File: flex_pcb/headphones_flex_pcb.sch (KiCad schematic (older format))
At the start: 14 parts, among them J1 LIGHTING_JACK, J3 BOTTOM_FLEX_LIGHTNING, J5 LIGHTNING_HEADPHONE_ADAPTER, J7 IPHONE_HEADPHONE_JACK, J8 CONN_01X02, U1 SN74LVC1G123, U2 ADG774A-LFCSP, U3 SN74LVC1G123, U4 NC7S32-micropak6

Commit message: About to try front fold
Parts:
- removed J8: CONN_01X02, Pin_Headers:Pin_Header_Straight_1x02_Pitch2.54mm, symbol CONN_01X02
- added J?: TEST_1P, symbol TEST_1P
- J3: footprint lightning_flex_pads:LIGHTNING_FLEX_PADS -> lightning_flex_pads:LIGHTNING_FLEX_PADS_NO_CRTYD
- renumbered R3 to R2, R2 to R3
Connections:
- net VCC: now also J?.1
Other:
- note removed: "TODO\nFigure out how to attach power"
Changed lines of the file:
@@
 F 0 "J3" H 9000 2850 60  0000 C CNN
 F 1 "BOTTOM_FLEX_LIGHTNING" H 9050 4050 60  0000 C CNN
-F 2 "lightning_flex_pads:LIGHTNING_FLEX_PADS" H 9000 3650 60  0001 C CNN
+F 2 "lightning_flex_pads:LIGHTNING_FLEX_PADS_NO_CRTYD" H 9000 3650 60  0001 C CNN
 F 3 "" H 9000 3650 60  0001 C CNN
 	1    9000 3650
@@
 $EndComp
 $Comp
-L R R2
+L R R3
 U 1 1 5925BA4D
 P 5250 3100
-F 0 "R2" V 5330 3100 50  0000 C CNN
+F 0 "R3" V 5330 3100 50  0000 C CNN
 F 1 "1M" V 5250 3100 50  0000 C CNN
 F 2 "Resistors_SMD:R_0201_NoSilk" V 5180 3100 50  0001 C CNN
@@
 $EndComp
 $Comp
-L R R3
+L R R2
 U 1 1 59264843
 P 5100 1250
-F 0 "R3" V 5180 1250 50  0000 C CNN
+F 0 "R2" V 5180 1250 50  0000 C CNN
 F 1 "100K" V 5100 1250 50  0000 C CNN
 F 2 "Resistors_SMD:R_0201_NoSilk" V 5030 1250 50  0001 C CNN
@@
 $EndComp
 $Comp
-L CONN_01X02 J8
-U 1 1 5926AC50
-P 9200 1700
-F 0 "J8" H 9200 1850 50  0000 C CNN
-F 1 "CONN_01X02" V 9300 1700 50  0000 C CNN
-F 2 "Pin_Headers:Pin_Header_Straight_1x02_Pitch2.54mm" H 9200 1700 50  0001 C CNN
-F 3 "" H 9200 1700 50  0001 C CNN
-	1    9200 1700
-	1    0    0    -1
-$EndComp
-$Comp
 L VCC #PWR013
 U 1 1 5926ACC1
-P 8900 1550
-F 0 "#PWR013" H 8900 1400 50  0001 C CNN
-F 1 "VCC" H 8900 1700 50  0000 C CNN
-F 2 "" H 8900 1550 50  0001 C CNN
-F 3 "" H 8900 1550 50  0001 C CNN
-	1    8900 1550
-	1    0    0    -1
-$EndComp
-$Comp
-L GNDREF #PWR014
-U 1 1 5926AD08
-P 8900 1850
-F 0 "#PWR014" H 8900 1600 50  0001 C CNN
-F 1 "GNDREF" H 8900 1700 50  0000 C CNN
-F 2 "" H 8900 1850 50  0001 C CNN
-F 3 "" H 8900 1850 50  0001 C CNN
-	1    8900 1850
+P 9800 1550
+F 0 "#PWR013" H 9800 1400 50  0001 C CNN
+F 1 "VCC" H 9800 1700 50  0000 C CNN
+F 2 "" H 9800 1550 50  0001 C CNN
+F 3 "" H 9800 1550 50  0001 C CNN
+	1    9800 1550
 	1    0    0    -1
 $EndComp
@@
 Wire Wire Line
 	2500 2000 3400 2000
-Wire Wire Line
-	8900 1650 8900 1550
-Wire Wire Line
-	9000 1650 8900 1650
-Wire Wire Line
-	8900 1750 8900 1850
-Wire Wire Line
-	9000 1750 8900 1750
 Connection ~ 2050 5850
 Wire Wire Line
@@
 Wire Wire Line
 	8550 3500 8650 3500
-Text Notes 8550 2400 0    89   ~ 0
-TODO\nFigure out how to attach power
 $Comp
 L ADG774A-LFCSP U2
@@
 	-1   0    0    -1
 $EndComp
+$Comp
+L TEST_1P J?
+U 1 1 593E2785
+P 9900 1650
+F 0 "J?" H 9900 1920 50  0000 C CNN
+F 1 "TEST_1P" H 9900 1850 50  0000 C CNN
+F 2 "" H 10100 1650 50  0001 C CNN
+F 3 "" H 10100 1650 50  0001 C CNN
+	1    9900 1650
+	0    1    1    0
+$EndComp
+Wire Wire Line
+	9900 1650 9800 1650
+Wire Wire Line
+	9800 1650 9800 1550
 $EndSCHEMATC

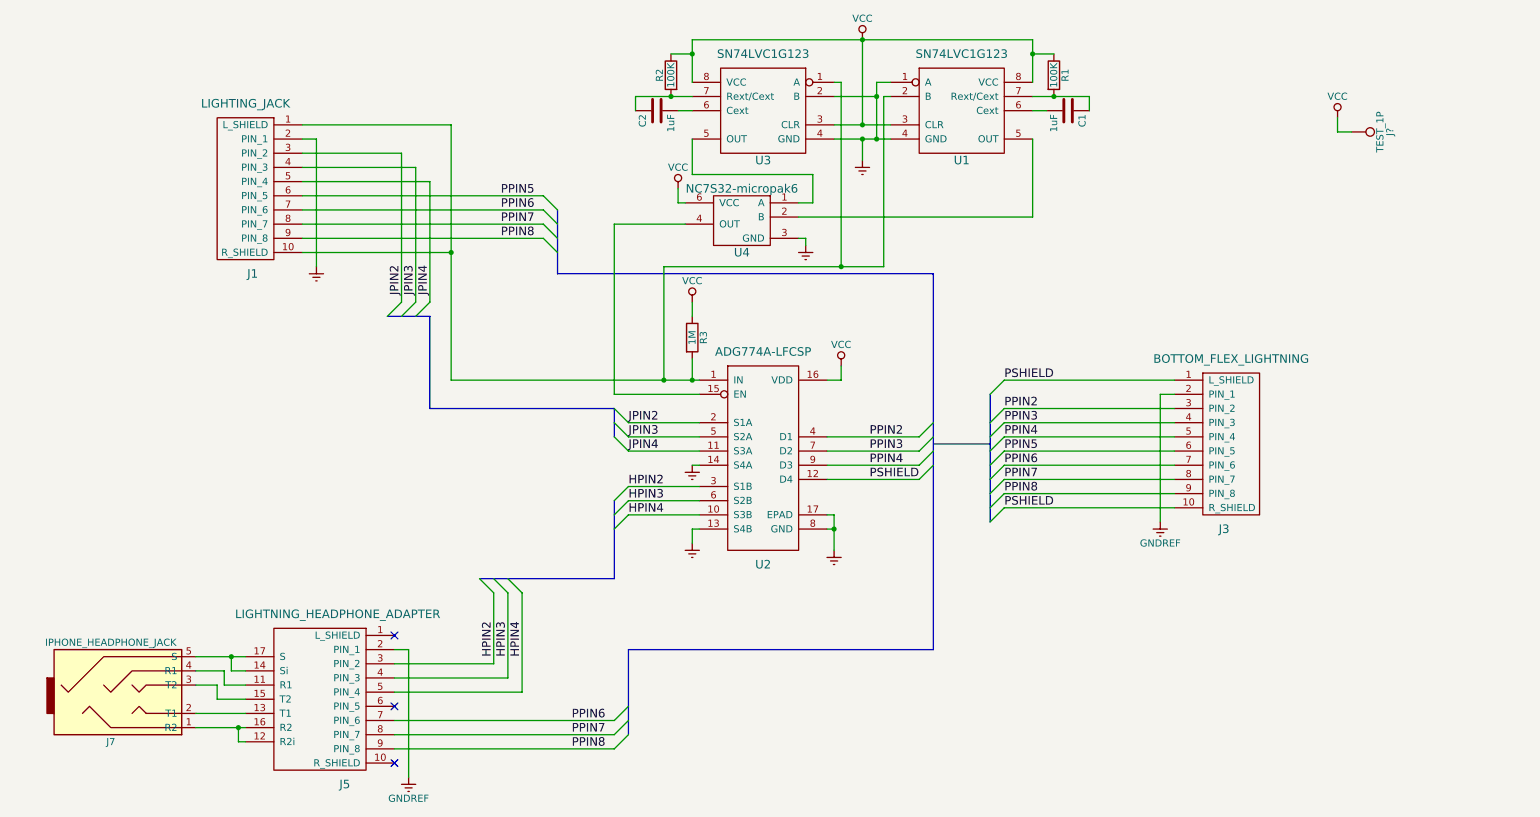
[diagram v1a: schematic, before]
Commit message: WIP: just before switching from 0201 -> 0402
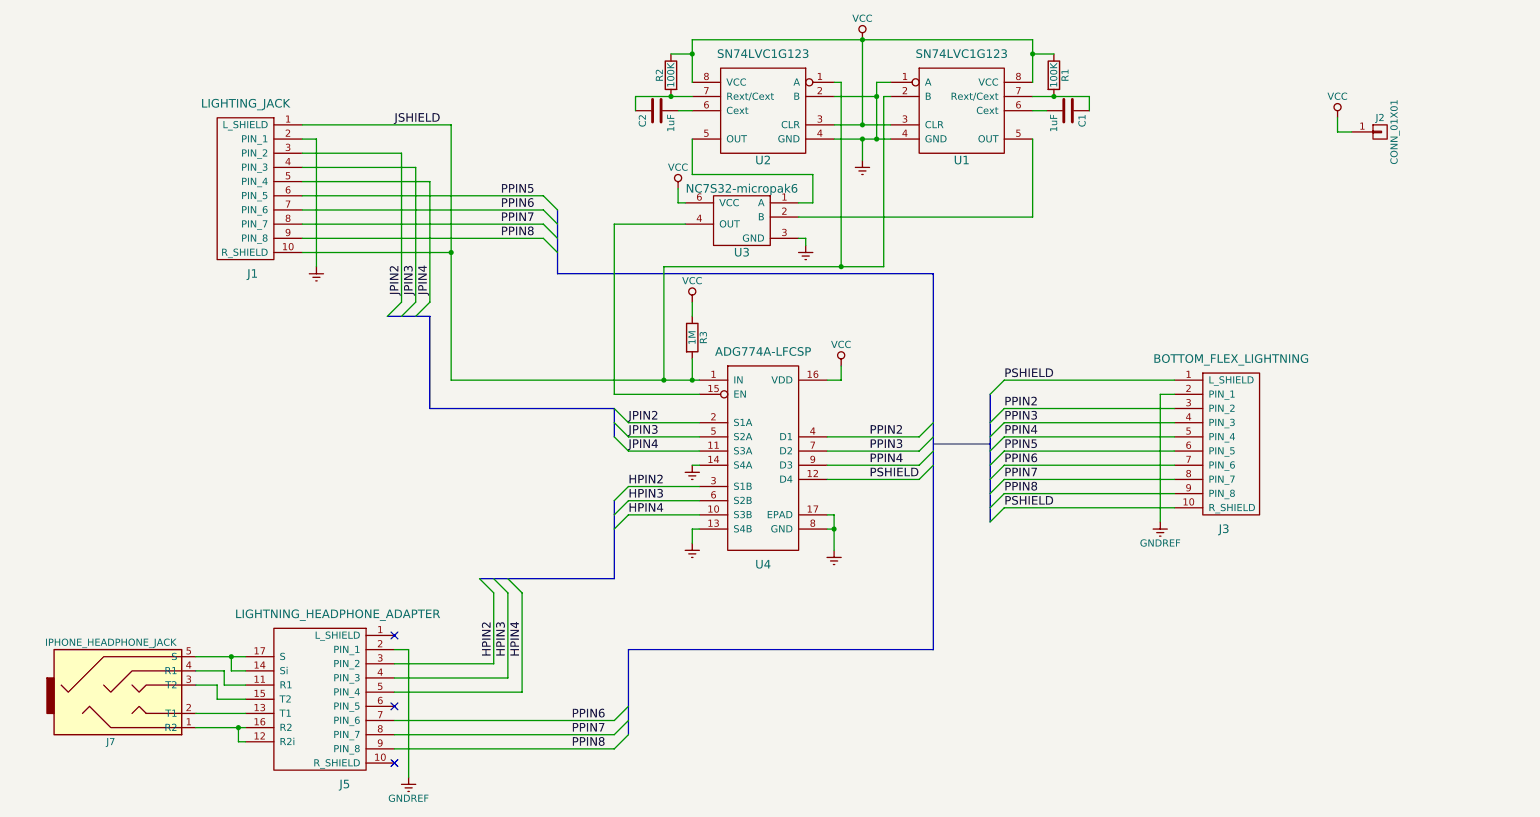
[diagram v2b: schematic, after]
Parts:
- removed J?: TEST_1P, symbol TEST_1P
- added J2: CONN_01X01, wire_pads:WIRE_PAD_2x3mm, symbol CONN_01X01
- J5: footprint lightning_headphone_adapter:LIGHTNING_HEADPHONE_ADAPTER -> lightning_headphone_adapter:LIGHTNING_HEADPHONE_ADAPTER_FRONT_FOLD
- renumbered U3 to U2, U4 to U3, U2 to U4
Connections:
- net VCC: now also J2.1 (P1)
- net JSHIELD: now reaches J1.1 (L_SHIELD), J1.10 (R_SHIELD), R3.2, U1.2 (B), U2.1 (A), U4.1 (IN)
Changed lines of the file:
@@
 $EndComp
 $Comp
-L SN74LVC1G123 U3
+L SN74LVC1G123 U2
 U 1 1 5926483D
 P 5750 1500
-F 0 "U3" H 5750 1150 60  0000 C CNN
+F 0 "U2" H 5750 1150 60  0000 C CNN
 F 1 "SN74LVC1G123" H 5750 1900 60  0000 C CNN
 F 2 "DSBGA-8:DSBGA-8_2x4_0.9x1.9mm_Pitch0.5mm_Dia0.25mm" H 5750 1100 60  0001 C CNN
@@
 F 0 "J5" H 2800 4650 60  0000 C CNN
 F 1 "LIGHTNING_HEADPHONE_ADAPTER" H 2850 5850 60  0000 C CNN
-F 2 "lightning_headphone_adapter:LIGHTNING_HEADPHONE_ADAPTER" H 2800 5450 60  0001 C CNN
+F 2 "lightning_headphone_adapter:LIGHTNING_HEADPHONE_ADAPTER_FRONT_FOLD" H 2800 5450 60  0001 C CNN
 F 3 "" H 2800 5450 60  0001 C CNN
 	1    2800 5450
@@
 	8550 3500 8650 3500
 $Comp
-L ADG774A-LFCSP U2
+L ADG774A-LFCSP U4
 U 1 1 592E4C1B
 P 5750 3950
-F 0 "U2" H 5750 3200 60  0000 C CNN
+F 0 "U4" H 5750 3200 60  0000 C CNN
 F 1 "ADG774A-LFCSP" H 5750 4700 60  0000 C CNN
 F 2 "Housings_DFN_QFN:QFN-16-1EP_3x3mm_Pitch0.5mm" H 5750 3950 60  0001 C CNN
@@
 Connection ~ 6250 4450
 $Comp
-L NC7S32-micropak6 U4
+L NC7S32-micropak6 U3
 U 1 1 592E5116
 P 5600 2250
-F 0 "U4" H 5600 2000 60  0000 C CNN
+F 0 "U3" H 5600 2000 60  0000 C CNN
 F 1 "NC7S32-micropak6" H 5600 2450 60  0000 C CNN
 F 2 "micropak6:Micropak6" H 5600 1750 60  0001 C CNN
@@
 	-1   0    0    -1
 $EndComp
-$Comp
-L TEST_1P J?
-U 1 1 593E2785
-P 9900 1650
-F 0 "J?" H 9900 1920 50  0000 C CNN
-F 1 "TEST_1P" H 9900 1850 50  0000 C CNN
-F 2 "" H 10100 1650 50  0001 C CNN
+Wire Wire Line
+	9900 1650 9800 1650
+Wire Wire Line
+	9800 1650 9800 1550
+$Comp
+L CONN_01X01 J2
+U 1 1 593E2C88
+P 10100 1650
+F 0 "J2" H 10100 1750 50  0000 C CNN
+F 1 "CONN_01X01" V 10200 1650 50  0000 C CNN
+F 2 "wire_pads:WIRE_PAD_2x3mm" H 10100 1650 50  0001 C CNN
 F 3 "" H 10100 1650 50  0001 C CNN
-	1    9900 1650
-	0    1    1    0
-$EndComp
-Wire Wire Line
-	9900 1650 9800 1650
-Wire Wire Line
-	9800 1650 9800 1550
+	1    10100 1650
+	1    0    0    -1
+$EndComp
+Text Label 3150 1600 0    60   ~ 0
+JSHIELD
 $EndSCHEMATC

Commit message: First flex pcb version - ready to fab. v0.9
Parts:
- C1, C2: footprint Capacitors_SMD:C_0201_NoSilk -> Capacitors_SMD:C_0402_NoSilk
- R1, R2, R3: footprint Resistors_SMD:R_0201_NoSilk -> Resistors_SMD:R_0402_NoSilk
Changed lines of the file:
@@
 F 0 "R3" V 5330 3100 50  0000 C CNN
 F 1 "1M" V 5250 3100 50  0000 C CNN
-F 2 "Resistors_SMD:R_0201_NoSilk" V 5180 3100 50  0001 C CNN
+F 2 "Resistors_SMD:R_0402_NoSilk" V 5180 3100 50  0001 C CNN
 F 3 "" H 5250 3100 50  0001 C CNN
 	1    5250 3100
@@
 F 0 "R1" V 7880 1250 50  0000 C CNN
 F 1 "100K" V 7800 1250 50  0000 C CNN
-F 2 "Resistors_SMD:R_0201_NoSilk" V 7730 1250 50  0001 C CNN
+F 2 "Resistors_SMD:R_0402_NoSilk" V 7730 1250 50  0001 C CNN
 F 3 "" H 7800 1250 50  0001 C CNN
 	1    7800 1250
@@
 F 0 "C1" H 7925 1600 50  0000 L CNN
 F 1 "1uF" H 7925 1400 50  0000 L CNN
-F 2 "Capacitors_SMD:C_0201_NoSilk" H 7938 1350 50  0001 C CNN
+F 2 "Capacitors_SMD:C_0402_NoSilk" H 7938 1350 50  0001 C CNN
 F 3 "" H 7900 1500 50  0001 C CNN
 	1    7900 1500
@@
 F 0 "R2" V 5180 1250 50  0000 C CNN
 F 1 "100K" V 5100 1250 50  0000 C CNN
-F 2 "Resistors_SMD:R_0201_NoSilk" V 5030 1250 50  0001 C CNN
+F 2 "Resistors_SMD:R_0402_NoSilk" V 5030 1250 50  0001 C CNN
 F 3 "" H 5100 1250 50  0001 C CNN
 	1    5100 1250
@@
 F 0 "C2" H 5025 1600 50  0000 L CNN
 F 1 "1uF" H 5025 1400 50  0000 L CNN
-F 2 "Capacitors_SMD:C_0201_NoSilk" H 5038 1350 50  0001 C CNN
+F 2 "Capacitors_SMD:C_0402_NoSilk" H 5038 1350 50  0001 C CNN
 F 3 "" H 5000 1500 50  0001 C CNN
 	1    5000 1500

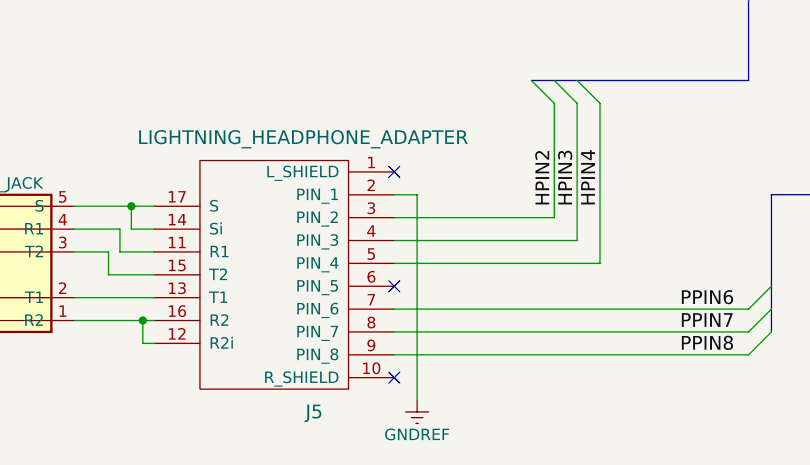
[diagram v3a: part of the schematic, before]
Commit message: Switch headphone adapter to handwired
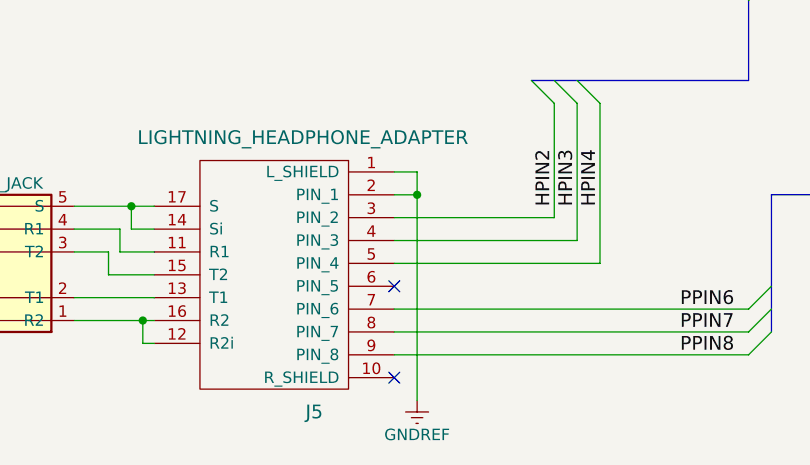
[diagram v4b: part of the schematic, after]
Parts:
- J5: footprint lightning_headphone_adapter:LIGHTNING_HEADPHONE_ADAPTER_FRONT_FOLD -> lightning_headphone_adapter:LIGHTNING_HEADPHONE_ADAPTER_HANDWIRE
- J7: footprint iphone_6s_headphone_jack:IPHONE_6S_HEADPHONE_JACK -> iphone_5_headphone_jack:IPHONE_5_HEADPHONE_JACK
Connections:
- net GNDREF: now also J5.1 (L_SHIELD)
- no-connect marks 3 -> 2
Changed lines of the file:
@@
 F 0 "J7" H 1150 5350 50  0000 C CNN
 F 1 "IPHONE_HEADPHONE_JACK" H 1150 6050 50  0000 C CNN
-F 2 "iphone_6s_headphone_jack:IPHONE_6S_HEADPHONE_JACK" H 1250 5500 50  0001 C CNN
+F 2 "iphone_5_headphone_jack:IPHONE_5_HEADPHONE_JACK" H 1250 5500 50  0001 C CNN
 F 3 "" H 1250 5500 50  0001 C CNN
 	1    1150 5650
@@
 F 0 "J5" H 2800 4650 60  0000 C CNN
 F 1 "LIGHTNING_HEADPHONE_ADAPTER" H 2850 5850 60  0000 C CNN
-F 2 "lightning_headphone_adapter:LIGHTNING_HEADPHONE_ADAPTER_FRONT_FOLD" H 2800 5450 60  0001 C CNN
+F 2 "lightning_headphone_adapter:LIGHTNING_HEADPHONE_ADAPTER_HANDWIRE" H 2800 5450 60  0001 C CNN
 F 3 "" H 2800 5450 60  0001 C CNN
 	1    2800 5450
@@
 	1    0    0    -1
 $EndComp
-NoConn ~ 3150 5200
 NoConn ~ 3150 5700
 NoConn ~ 3150 6100
@@
 	3850 5400 3850 4900
 Wire Wire Line
-	3250 5300 3250 6200
+	3250 5200 3250 6200
 Wire Wire Line
 	3150 5300 3250 5300
@@
 Text Label 3150 1600 0    60   ~ 0
 JSHIELD
+Wire Wire Line
+	3150 5200 3250 5200
+Connection ~ 3250 5300
 $EndSCHEMATC

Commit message: v0.17
I redesigned the flex pcb to use the TS3A5018 chip
for switching instead of the ADG774A.  This supports
a 3v signal, whereas the ADG774A only supported up
to 1.5v.  Also a bunch of minor tweaks to the board
design to make it easier to assemble and test (added
test pads!)

Also made a rigid version of the flex pcb, to help
debug manufacturing defects if necessary.
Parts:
- removed U4: ADG774A-LFCSP, Housings_DFN_QFN:QFN-16-1EP_3x3mm_Pitch0.5mm, symbol ADG774A-LFCSP
- added T_EN1, T_IN1, T_J2, T_J3, T_J4, T_JS1, T_P2, T_P3, T_P4, T_P5, T_PS1, T_R1, T_R2, T_S1, T_T1, T_T2, T_U1, T_U2: TEST, testpoints:testpoint_1mm, symbol TEST
- added U4: TS3Y5018RSV-UQFN, PUQFN-N16:R-PUQFN-N16, symbol TS3Y5018RSV-UQFN
- J1: footprint lightning_jack:LIGHTNING_JACK -> lightning_jack:LIGHTNING_JACK_NO_LEFT_HOLES
- U1, U2: symbol SN74LVC1G123 -> SN74LVC1G123-RESCUE-headphones_flex_pcb
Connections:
- net GNDREF: now also U4.11 (NO4), U4.12 (NC4), U4.6 (GND)
- net HPIN2: now also U4.1 (NO1)
- net HPIN3: now also U4.4 (NO2)
- net HPIN4: now also U4.8 (NO3)
- net JPIN2: now also T_J2.1, U4.16 (NC1)
- net JPIN3: now also T_J3.1, U4.3 (NC2)
- net JPIN4: now also T_J4.1, U4.9 (NC3)
- net JSHIELD: now also T_IN1.1, T_JS1.1, U4.15 (IN)
- net PPIN2: now also T_P2.1, U4.2 (COM1)
- net PPIN3: now also T_P3.1, U4.5 (COM2)
- net PPIN4: now also T_P4.1, U4.7 (COM3)
- net PPIN5: now also T_P5.1
- net PSHIELD: now also T_PS1.1, U4.10 (COM4)
- net VCC: now also U4.14 (V+)
- net at U1.5 (OUT), U3.2 (B): now also T_U1.1
- net at U2.5 (OUT), U3.1 (A): now also T_U2.1
- net at J5.12 (R2i), J5.16 (R2), J7.1 (R2): now also T_R2.1
- net at J5.13 (T1), J7.2 (T1): now also T_T1.1
- net at J5.15 (T2), J7.3 (T2): now also T_T2.1
- net at J5.11 (R1), J7.4 (R1): now also T_R1.1
- net at J5.14 (Si), J5.17 (S), J7.5 (S): now also T_S1.1
- net at U3.4 (OUT): now also T_EN1.1, U4.13 (EN)
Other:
- moved on the sheet: C1, C2, J1, J2, J3, J5, J7, R1, R2, R3, U1, U2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
